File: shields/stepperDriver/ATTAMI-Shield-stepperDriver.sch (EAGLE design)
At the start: 11 parts

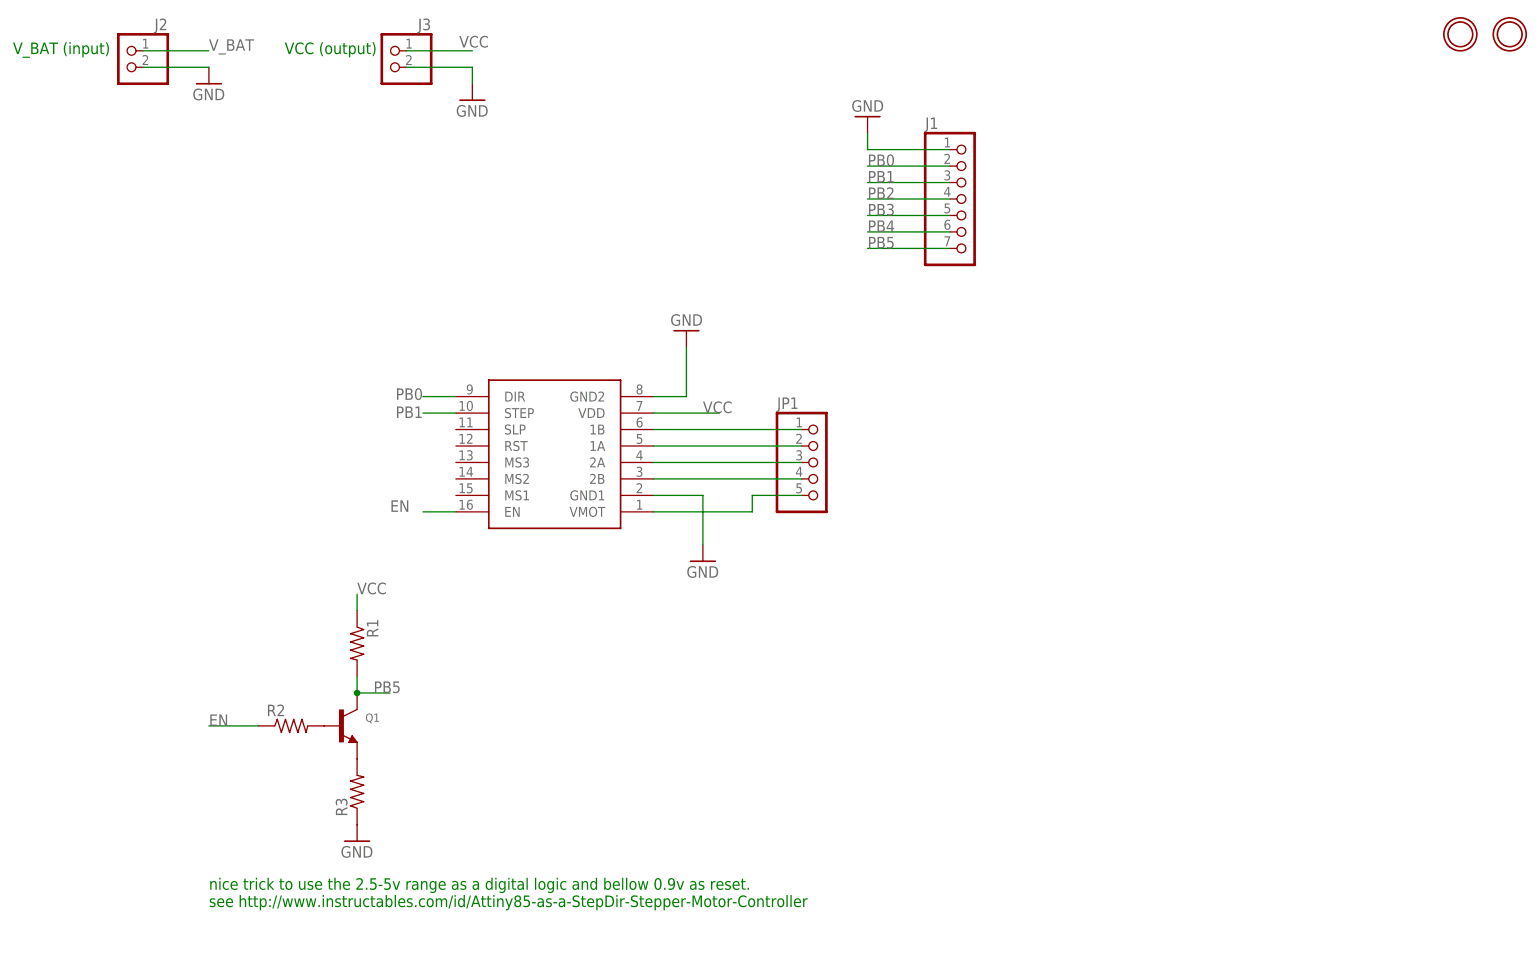
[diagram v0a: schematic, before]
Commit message: cont work on stepper shield
mostly done, could work if we agree on V_BAT to 12V
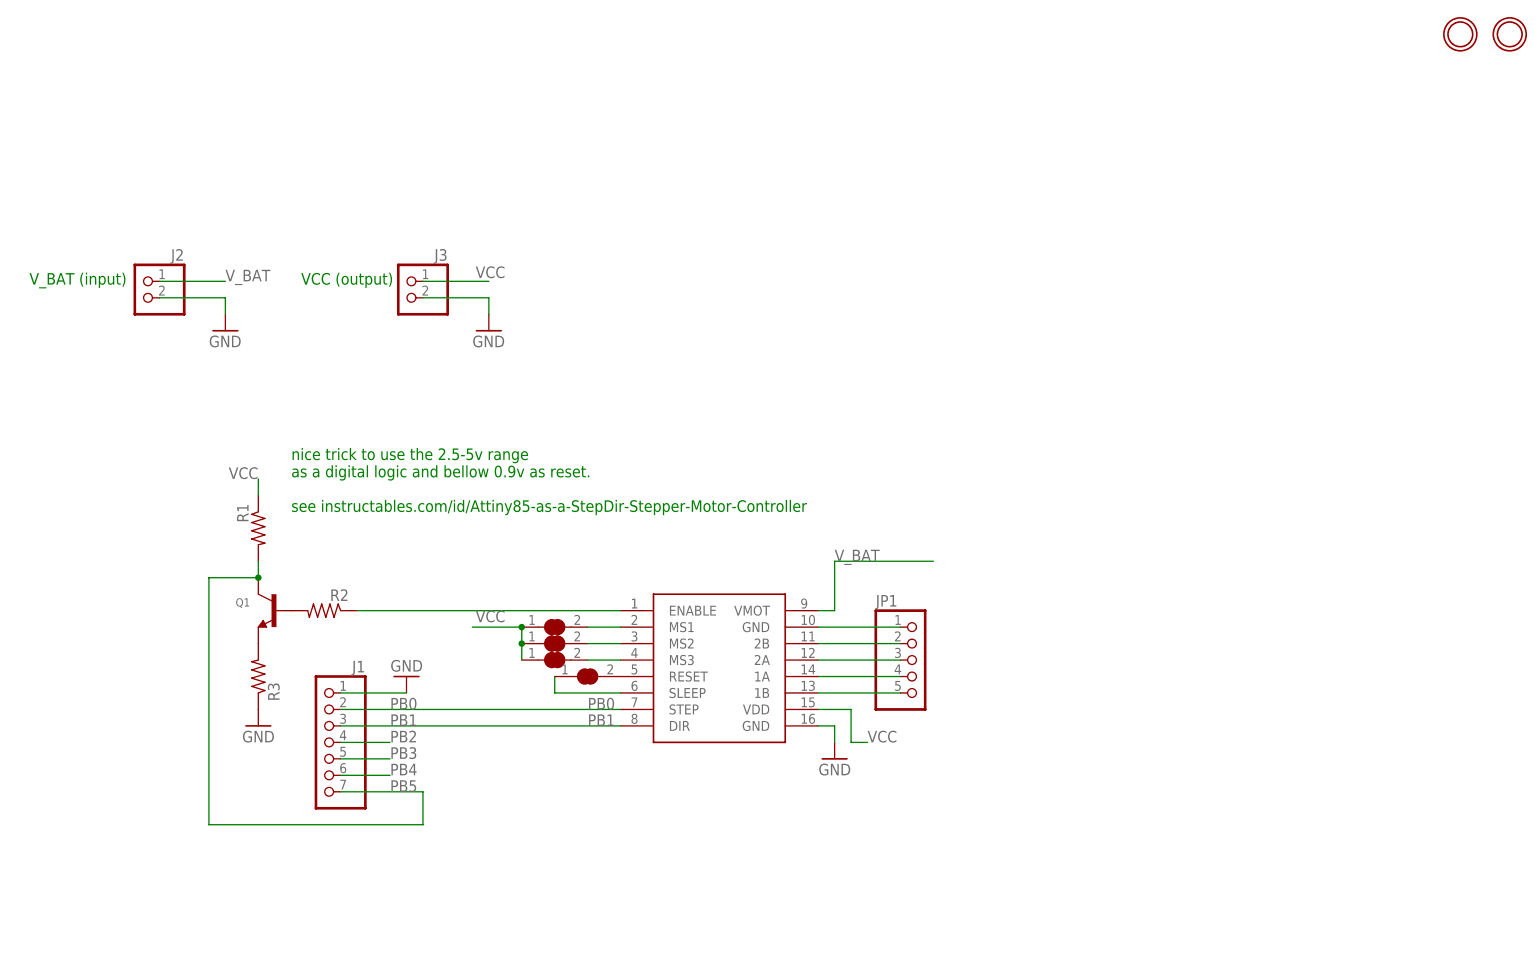
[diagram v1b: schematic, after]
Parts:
- removed U$4: POLOLUESTEPPERDRIVER, reprap:POLOLUESTEPPERDRIVER
- added SJ1, SJ2, SJ3, SJ4: (no value), microbuilder:SOLDERJUMPER_CLOSED
- added U$3: STEPPER_driver, ATtami:STEPPERDRIVER_A4988
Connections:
- removed net EN: R2.1, U$4.EN
- removed net N$11: JP1.2, U$4.1A
- new net ENABLE: R2.1, U$3.ENABLE
- new net N$14: SJ1.2, U$3.MS3
- new net N$2: SJ4.2, U$3.RESET
- new net N$3: JP1.2, U$3.2B
- new net N$6: JP1.3, U$3.2A
- new net N$7: JP1.4, U$3.1A
- new net N$9: SJ4.1, U$3.SLEEP
- net GND: now also JP1.1, U$3.GND@1, U$3.GND@2; no longer U$4.GND1, U$4.GND2
- net N$10: now also SJ3.2, U$3.MS1; no longer JP1.3, U$4.2A
- net N$13: now also SJ2.2, U$3.MS2; no longer JP1.1, U$4.1B
- net N$8: now also JP1.5, U$3.1B; no longer JP1.4, U$4.2B
- net PB0: now also U$3.STEP; no longer U$4.DIR
- net PB1: now also U$3.DIR; no longer U$4.STEP
- net VCC: now also SJ1.1, SJ2.1, SJ3.1, U$3.VDD; no longer U$4.VDD
- net V_BAT: now also U$3.VMOT; no longer JP1.5, U$4.VMOT
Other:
- note added: "nice trick to use the 2.5-5v range as a digital logic and bellow 0.9v as reset. see instructables.com/id/Attiny85-as-a-StepDir-Stepper-Motor-Controller"
- note removed: "nice trick to use the 2.5-5v range as a digital logic and bellow 0.9v as reset. see http://www.instructables.com/id/Attiny85-as-a-StepDir-Stepper-Motor-Controller"
- moved on the sheet: J1, J2, J3, JP1, Q1, R1, R2, R3

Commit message: updtae A4988 lib part
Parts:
- BRK1: value STEPPER_driver -> A4988_driver
- renumbered U$3 to BRK1
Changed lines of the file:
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@@
 <part name="SJ2" library="microbuilder" deviceset="SOLDERJUMPER_CLOSED" device=""/>
 <part name="SJ3" library="microbuilder" deviceset="SOLDERJUMPER_CLOSED" device=""/>
-<part name="U$3" library="ATtami" deviceset="STEPPERDRIVER_A4988" device="" value="STEPPER_driver"/>
+<part name="BRK1" library="ATtami" deviceset="STEPPERDRIVER_A4988" device="" value="A4988_driver"/>
 <part name="SJ4" library="microbuilder" deviceset="SOLDERJUMPER_CLOSED" device=""/>
 </parts>
@@
 <attribute name="VALUE" x="91.44" y="72.39" size="1.778" layer="96"/>
 </instance>
-<instance part="U$3" gate="G$1" x="119.38" y="71.12"/>
+<instance part="BRK1" gate="G$1" x="119.38" y="71.12"/>
 <instance part="SJ4" gate="G$1" x="99.06" y="68.58" smashed="yes">
 <attribute name="VALUE" x="96.52" y="64.77" size="1.778" layer="96"/>
@@
 <wire x1="137.16" y1="60.96" x2="137.16" y2="58.42" width="0.1524" layer="91"/>
 <pinref part="GND3" gate="1" pin="GND"/>
-<pinref part="U$3" gate="G$1" pin="GND@1"/>
+<pinref part="BRK1" gate="G$1" pin="GND@1"/>
 </segment>
 <segment>
 <wire x1="134.62" y1="76.2" x2="147.32" y2="76.2" width="0.1524" layer="91"/>
-<pinref part="U$3" gate="G$1" pin="GND@2"/>
+<pinref part="BRK1" gate="G$1" pin="GND@2"/>
 <pinref part="JP1" gate="A" pin="1"/>
 </segment>
@@
 <wire x1="139.7" y1="58.42" x2="142.24" y2="58.42" width="0.1524" layer="91"/>
 <label x="142.24" y="58.42" size="1.778" layer="95"/>
-<pinref part="U$3" gate="G$1" pin="VDD"/>
+<pinref part="BRK1" gate="G$1" pin="VDD"/>
 </segment>
 <segment>
@@
 </segment>
 <segment>
-<pinref part="U$3" gate="G$1" pin="VMOT"/>
+<pinref part="BRK1" gate="G$1" pin="VMOT"/>
 <wire x1="134.62" y1="78.74" x2="137.16" y2="78.74" width="0.1524" layer="91"/>
 <wire x1="137.16" y1="78.74" x2="137.16" y2="86.36" width="0.1524" layer="91"/>
@@
 <pinref part="J1" gate="A" pin="2"/>
 <label x="68.58" y="63.5" size="1.778" layer="95"/>
-<pinref part="U$3" gate="G$1" pin="STEP"/>
+<pinref part="BRK1" gate="G$1" pin="STEP"/>
 </segment>
 </net>
@@
 <label x="99.06" y="60.96" size="1.778" layer="95"/>
 <wire x1="60.96" y1="60.96" x2="104.14" y2="60.96" width="0.1524" layer="91"/>
-<pinref part="U$3" gate="G$1" pin="DIR"/>
+<pinref part="BRK1" gate="G$1" pin="DIR"/>
 </segment>
 </net>
@@
 <pinref part="R2" gate="G$1" pin="1"/>
 <wire x1="63.5" y1="78.74" x2="104.14" y2="78.74" width="0.1524" layer="91"/>
-<pinref part="U$3" gate="G$1" pin="ENABLE"/>
+<pinref part="BRK1" gate="G$1" pin="ENABLE"/>
 </segment>
 </net>
@@
 <wire x1="104.14" y1="76.2" x2="99.06" y2="76.2" width="0.1524" layer="91"/>
 <pinref part="SJ3" gate="G$1" pin="2"/>
-<pinref part="U$3" gate="G$1" pin="MS1"/>
+<pinref part="BRK1" gate="G$1" pin="MS1"/>
 </segment>
 </net>
@@
 <wire x1="104.14" y1="73.66" x2="99.06" y2="73.66" width="0.1524" layer="91"/>
 <pinref part="SJ2" gate="G$1" pin="2"/>
-<pinref part="U$3" gate="G$1" pin="MS2"/>
+<pinref part="BRK1" gate="G$1" pin="MS2"/>
 </segment>
 </net>
@@
 <wire x1="104.14" y1="71.12" x2="99.06" y2="71.12" width="0.1524" layer="91"/>
 <pinref part="SJ1" gate="G$1" pin="2"/>
-<pinref part="U$3" gate="G$1" pin="MS3"/>
+<pinref part="BRK1" gate="G$1" pin="MS3"/>
 </segment>
 </net>
@@
 <pinref part="JP1" gate="A" pin="2"/>
 <wire x1="147.32" y1="73.66" x2="134.62" y2="73.66" width="0.1524" layer="91"/>
-<pinref part="U$3" gate="G$1" pin="2B"/>
+<pinref part="BRK1" gate="G$1" pin="2B"/>
 </segment>
 </net>
@@
 <pinref part="JP1" gate="A" pin="3"/>
 <wire x1="134.62" y1="71.12" x2="147.32" y2="71.12" width="0.1524" layer="91"/>
-<pinref part="U$3" gate="G$1" pin="2A"/>
+<pinref part="BRK1" gate="G$1" pin="2A"/>
 </segment>
 </net>
@@
 <pinref part="JP1" gate="A" pin="4"/>
 <wire x1="147.32" y1="68.58" x2="134.62" y2="68.58" width="0.1524" layer="91"/>
-<pinref part="U$3" gate="G$1" pin="1A"/>
+<pinref part="BRK1" gate="G$1" pin="1A"/>
 </segment>
 </net>
@@
 <pinref part="JP1" gate="A" pin="5"/>
 <wire x1="134.62" y1="66.04" x2="147.32" y2="66.04" width="0.1524" layer="91"/>
-<pinref part="U$3" gate="G$1" pin="1B"/>
+<pinref part="BRK1" gate="G$1" pin="1B"/>
 </segment>
 </net>
 <net name="N$2" class="0">
 <segment>
-<pinref part="U$3" gate="G$1" pin="RESET"/>
+<pinref part="BRK1" gate="G$1" pin="RESET"/>
 <pinref part="SJ4" gate="G$1" pin="2"/>
 </segment>
@@
 <pinref part="SJ4" gate="G$1" pin="1"/>
 <wire x1="93.98" y1="68.58" x2="93.98" y2="66.04" width="0.1524" layer="91"/>
-<pinref part="U$3" gate="G$1" pin="SLEEP"/>
+<pinref part="BRK1" gate="G$1" pin="SLEEP"/>
 <wire x1="93.98" y1="66.04" x2="104.14" y2="66.04" width="0.1524" layer="91"/>
 </segment>

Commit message: addded 4pin header for 12+ and I2C, not routed
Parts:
- added CN1: 1X4-BIG, adafruit:1X4-BIG
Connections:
- net GND: now also CN1.2
- net PB3: now also CN1.4
- net PB4: now also CN1.3
- net V_BAT: now also CN1.1
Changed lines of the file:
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@@
 <part name="BRK1" library="ATtami" deviceset="STEPPERDRIVER_A4988" device="" value="A4988_driver"/>
 <part name="SJ4" library="microbuilder" deviceset="SOLDERJUMPER_CLOSED" device=""/>
+<part name="CN1" library="adafruit" deviceset="1X4" device="-BIG"/>
+<part name="GND4" library="SparkFun" deviceset="GND" device=""/>
 </parts>
 <sheets>
@@
 <attribute name="VALUE" x="96.52" y="64.77" size="1.778" layer="96"/>
 </instance>
+<instance part="CN1" gate="G$1" x="99.06" y="38.1"/>
+<instance part="GND4" gate="1" x="86.36" y="48.26" rot="MR180"/>
 </instances>
 <busses>
@@
 <pinref part="BRK1" gate="G$1" pin="GND@2"/>
 <pinref part="JP1" gate="A" pin="1"/>
+</segment>
+<segment>
+<pinref part="GND4" gate="1" pin="GND"/>
+<wire x1="86.36" y1="45.72" x2="86.36" y2="38.1" width="0.1524" layer="91"/>
+<pinref part="CN1" gate="G$1" pin="2"/>
+<wire x1="86.36" y1="38.1" x2="93.98" y2="38.1" width="0.1524" layer="91"/>
 </segment>
 </net>
@@
 <label x="137.16" y="86.36" size="1.778" layer="95"/>
 </segment>
+<segment>
+<pinref part="CN1" gate="G$1" pin="1"/>
+<wire x1="93.98" y1="40.64" x2="91.44" y2="40.64" width="0.1524" layer="91"/>
+<wire x1="91.44" y1="40.64" x2="91.44" y2="45.72" width="0.1524" layer="91"/>
+<label x="91.44" y="45.72" size="1.778" layer="95"/>
+</segment>
 </net>
 <net name="PB0" class="0">
@@
 <segment>
 <pinref part="J1" gate="A" pin="4"/>
+<label x="68.58" y="58.42" size="1.778" layer="95"/>
 <wire x1="60.96" y1="58.42" x2="68.58" y2="58.42" width="0.1524" layer="91"/>
-<label x="68.58" y="58.42" size="1.778" layer="95"/>
 </segment>
 </net>
@@
 <segment>
 <pinref part="J1" gate="A" pin="5"/>
-<wire x1="68.58" y1="55.88" x2="60.96" y2="55.88" width="0.1524" layer="91"/>
 <label x="68.58" y="55.88" size="1.778" layer="95"/>
+<wire x1="60.96" y1="55.88" x2="78.74" y2="55.88" width="0.1524" layer="91"/>
+<pinref part="CN1" gate="G$1" pin="4"/>
+<wire x1="93.98" y1="33.02" x2="78.74" y2="33.02" width="0.1524" layer="91"/>
+<wire x1="78.74" y1="33.02" x2="78.74" y2="55.88" width="0.1524" layer="91"/>
 </segment>
 </net>
@@
 <segment>
 <pinref part="J1" gate="A" pin="6"/>
-<wire x1="68.58" y1="53.34" x2="60.96" y2="53.34" width="0.1524" layer="91"/>
 <label x="68.58" y="53.34" size="1.778" layer="95"/>
-</segment>
-</net>
+<wire x1="81.28" y1="53.34" x2="60.96" y2="53.34" width="0.1524" layer="91"/>
+<pinref part="CN1" gate="G$1" pin="3"/>
+<wire x1="81.28" y1="35.56" x2="93.98" y2="35.56" width="0.1524" layer="91"/>
+<wire x1="81.28" y1="53.34" x2="81.28" y2="35.56" width="0.1524" layer="91"/>
+</segment>
+</net>

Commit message: updated wiring, needs review
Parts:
- BRK1: device ATtami:STEPPERDRIVER_A4988 -> ATtami:A4988_DRIVER
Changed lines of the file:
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@@
 <part name="SJ2" library="microbuilder" deviceset="SOLDERJUMPER_CLOSED" device=""/>
 <part name="SJ3" library="microbuilder" deviceset="SOLDERJUMPER_CLOSED" device=""/>
-<part name="BRK1" library="ATtami" deviceset="STEPPERDRIVER_A4988" device="" value="A4988_driver"/>
+<part name="BRK1" library="ATtami" deviceset="A4988_DRIVER" device="" value="A4988_driver"/>
 <part name="SJ4" library="microbuilder" deviceset="SOLDERJUMPER_CLOSED" device=""/>
 <part name="CN1" library="adafruit" deviceset="1X4" device="-BIG"/>

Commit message: simplfy
this is a driver design we need a barebone onn with High Speed
Optoisolator SOIC 16 , 60V 4A.
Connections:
- removed net ENABLE: BRK1.ENABLE, R2.1
- net PB2: now also BRK1.ENABLE
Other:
- note added: "I2C"
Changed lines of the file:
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@@
 as a digital logic and bellow 0.9v as reset.
 see instructables.com/id/Attiny85-as-a-StepDir-Stepper-Motor-Controller</text>
+<text x="84.328" y="29.718" size="1.778" layer="91">I2C</text>
 </plain>
 <instances>
@@
 <pinref part="J1" gate="A" pin="4"/>
 <label x="68.58" y="58.42" size="1.778" layer="95"/>
-<wire x1="60.96" y1="58.42" x2="68.58" y2="58.42" width="0.1524" layer="91"/>
+<wire x1="60.96" y1="58.42" x2="76.2" y2="58.42" width="0.1524" layer="91"/>
+<wire x1="76.2" y1="58.42" x2="76.2" y2="78.74" width="0.1524" layer="91"/>
+<pinref part="BRK1" gate="G$1" pin="ENABLE"/>
+<wire x1="76.2" y1="78.74" x2="104.14" y2="78.74" width="0.1524" layer="91"/>
 </segment>
 </net>
@@
 </segment>
 </net>
-<net name="ENABLE" class="0">
-<segment>
-<pinref part="R2" gate="G$1" pin="1"/>
-<wire x1="63.5" y1="78.74" x2="104.14" y2="78.74" width="0.1524" layer="91"/>
-<pinref part="BRK1" gate="G$1" pin="ENABLE"/>
-</segment>
-</net>
